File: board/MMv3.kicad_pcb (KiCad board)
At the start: 2 copper layers, 53 parts, among them J1 PWR, J2 SWD, J3 left_mot, J4 DRV8833_L, J5 right_mot, J6 DRV8833_R, Q1 DMG2301L, Q2 DMG2302U, Q3 DMG2302U, Q4 DMG2302U, SW1 but, U1 LSM9DS1, U2 LD1117S50TR_SOT223, U3 DS28E05R+T, U4 RPi_Pico

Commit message: Finished layout
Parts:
- added H1: MountingHole, MountingHole:MountingHole_3.2mm_M3_Pad_TopBottom, F.Cu at (168.0, 95.0)
- D10, D11, D12, D13, D2, D3, D4, D5, D6, D7, D8, D9, J3, J5: moved to B.Cu
- moved Q3 125.1 mm to (165.0, 79.8), turned to 90 degrees
- moved D9 125.1 mm to (166.0, 76.5), turned to 90 degrees
- moved R11 119.3 mm to (165.0, 83.8), turned to 180 degrees
- moved D7 118.7 mm to (166.0, 73.5), turned to 90 degrees
- moved R12 116.1 mm to (165.0, 82.2)
- moved C1 114.9 mm to (173.0, 108.8), turned to 90 degrees
- moved R14 112.5 mm to (168.2, 75.0), turned to 90 degrees
- moved C3 112.4 mm to (167.2, 118.0), turned to 90 degrees
- moved C7 111.7 mm to (171.5, 108.8), turned to 90 degrees
- moved D13 111.3 mm to (177.2, 101.0)
- moved R17 110.4 mm to (178.8, 78.2)
- moved Q4 110.2 mm to (174.0, 75.0)
- moved C2 108.4 mm to (170.0, 108.8), turned to 90 degrees
- moved D12 108.3 mm to (177.2, 76.0)
- moved C5 106.6 mm to (167.5, 112.5), turned to 180 degrees
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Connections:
- J6 pad 2: /lmot_m2 -> /lmot_m1
- J6 pad 3: /lmot_m1 -> /lmot_m2
- J6 pad 4: /rmot_m2 -> /rmot_m1
- J6 pad 5: /rmot_m1 -> /rmot_m2
- R4 pad 2: /r_adc -> /c_adc
- R5 pad 2: /c_adc -> /r_adc
- U4 pad 10: /rir_b -> /lir_b
- U4 pad 11: /rir_en -> /lir_en
- U4 pad 12: /cir_a -> /rir_b
- U4 pad 14: /cir_b -> /rir_a
- U4 pad 15: /cir_en -> /rir_en
- U4 pad 16: /lenc_a -> /cir_a
- U4 pad 17: /lenc_b -> /cir_en
- U4 pad 19: /renc_a -> /cir_b
- U4 pad 20: /renc_b -> Net-(U4-Pad20)
- U4 pad 21: /rmot_in2 -> /lenc_a
- U4 pad 22: /rmot_in1 -> /lenc_b
- U4 pad 24: /lmot_in2 -> /renc_a
- U4 pad 25: /lmot_in1 -> /renc_b
- U4 pad 26: /lir_a -> /rmot_in2
- U4 pad 27: /lir_b -> /rmot_in1
- U4 pad 29: /lir_en -> /lmot_in2
- U4 pad 31: /r_adc -> /c_adc
- U4 pad 32: /c_adc -> /r_adc
- U4 pad 7: Net-(U4-Pad7) -> /lmot_in1
- U4 pad 9: /rir_a -> /lir_a
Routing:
- net +5V: track 0.00 -> 159.0 mm, vias 0 -> 2
- net +3V3: track 0.00 -> 111.8 mm, vias 0 -> 5
- net /r_adc: track 0.00 -> 67.0 mm, vias 0 -> 1
- net /lir_b: track 0.00 -> 63.3 mm
- net /c_adc: track 0.00 -> 61.4 mm
- net /lir_en: track 0.00 -> 55.7 mm, vias 0 -> 1
- net /l_adc: track 0.00 -> 49.5 mm, vias 0 -> 1
- net /lir_a: track 0.00 -> 38.1 mm, vias 0 -> 2
- net Net-(D6-Pad1): track 0.00 -> 36.5 mm
- net /cir_a: track 0.00 -> 34.3 mm
- net /RST: track 0.00 -> 34.1 mm
- net Net-(D2-Pad1): track 0.00 -> 33.1 mm
- net /rmot_in2: track 0.00 -> 33.1 mm
- net /rir_a: track 0.00 -> 33.0 mm
- net Net-(D10-Pad1): track 0.00 -> 32.4 mm
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- added copper zone on B.Cu, net GND
- added copper zone on F.Cu, net GND
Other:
- board outline added: 64 x 54 mm
- net class Power added: clearance 0.2, trace_width 0.32, via_dia 0.6, via_drill 0.3
- board text added: "MMv3 R1 Matthew Tran"

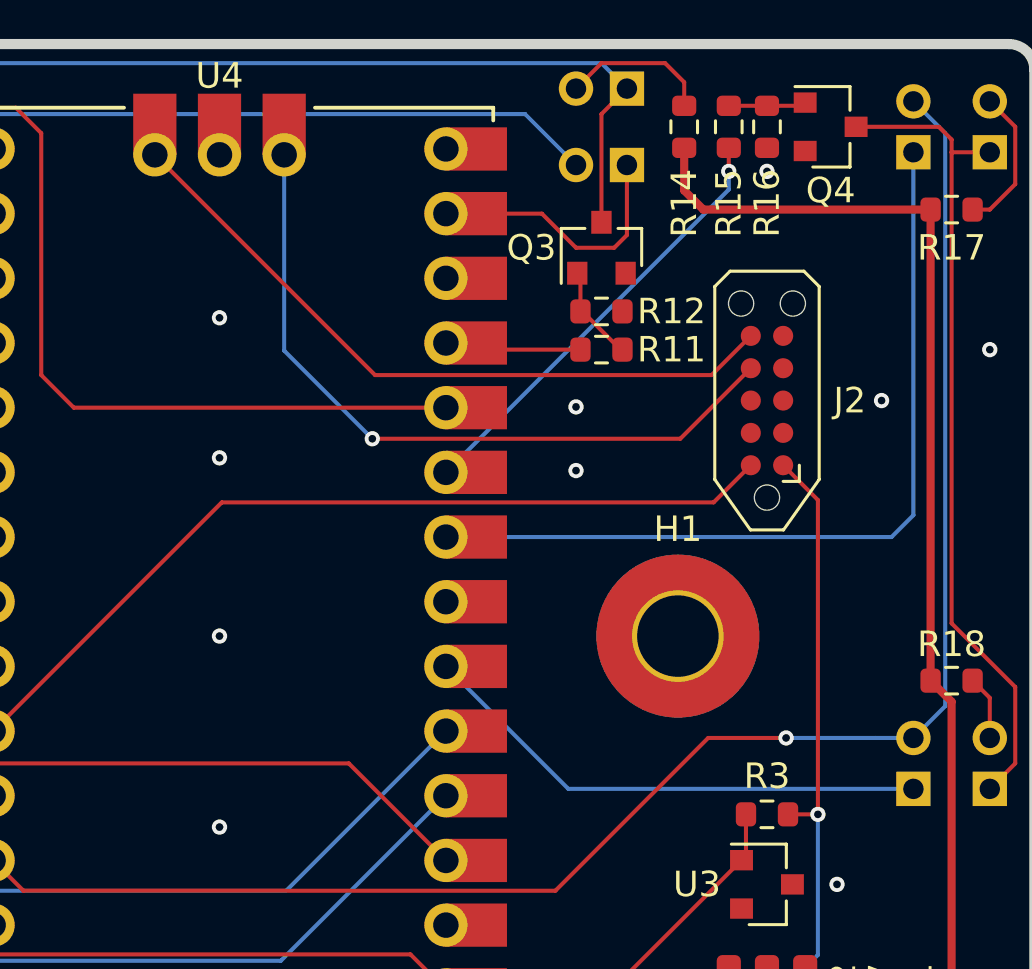
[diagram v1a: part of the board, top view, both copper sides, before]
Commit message: Fixed SWD pinout
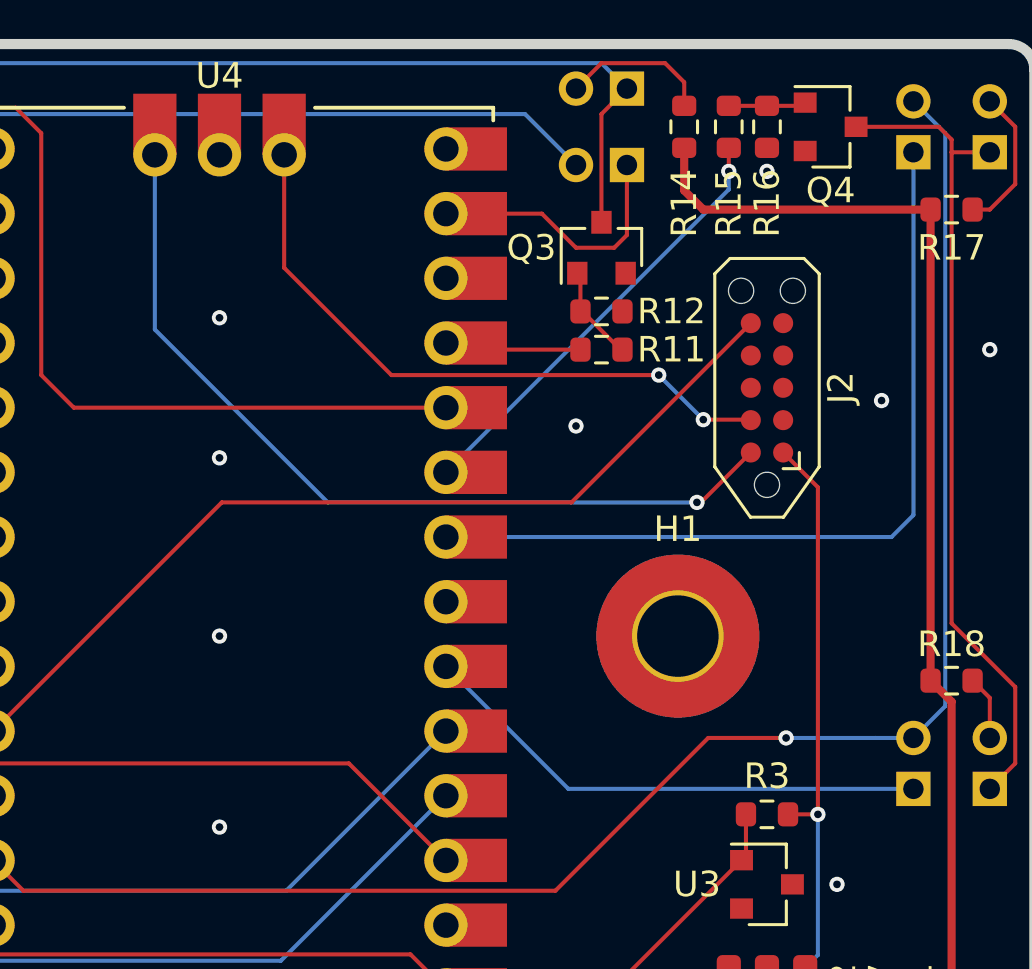
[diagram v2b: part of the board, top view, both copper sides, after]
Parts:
- moved J2 0.50 mm to (171.5, 85.2)
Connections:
- J2 pad 10: /RST -> /SWDIO
- J2 pad 6: /SWDIO -> /RST
- J2 pad 7: /SWCLK -> Net-(J2-Pad7)
- J2 pad 9: Net-(J2-Pad9) -> /SWCLK
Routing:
- net /SWDIO: track 27.6 -> 33.9 mm, vias 0 -> 1
- net /SWCLK: track 28.6 -> 25.2 mm, vias 1 -> 2
- net /RST: track 34.1 -> 36.4 mm
- net +3V3: track 111.8 -> 112.3 mm
- net GND: vias 19 -> 18

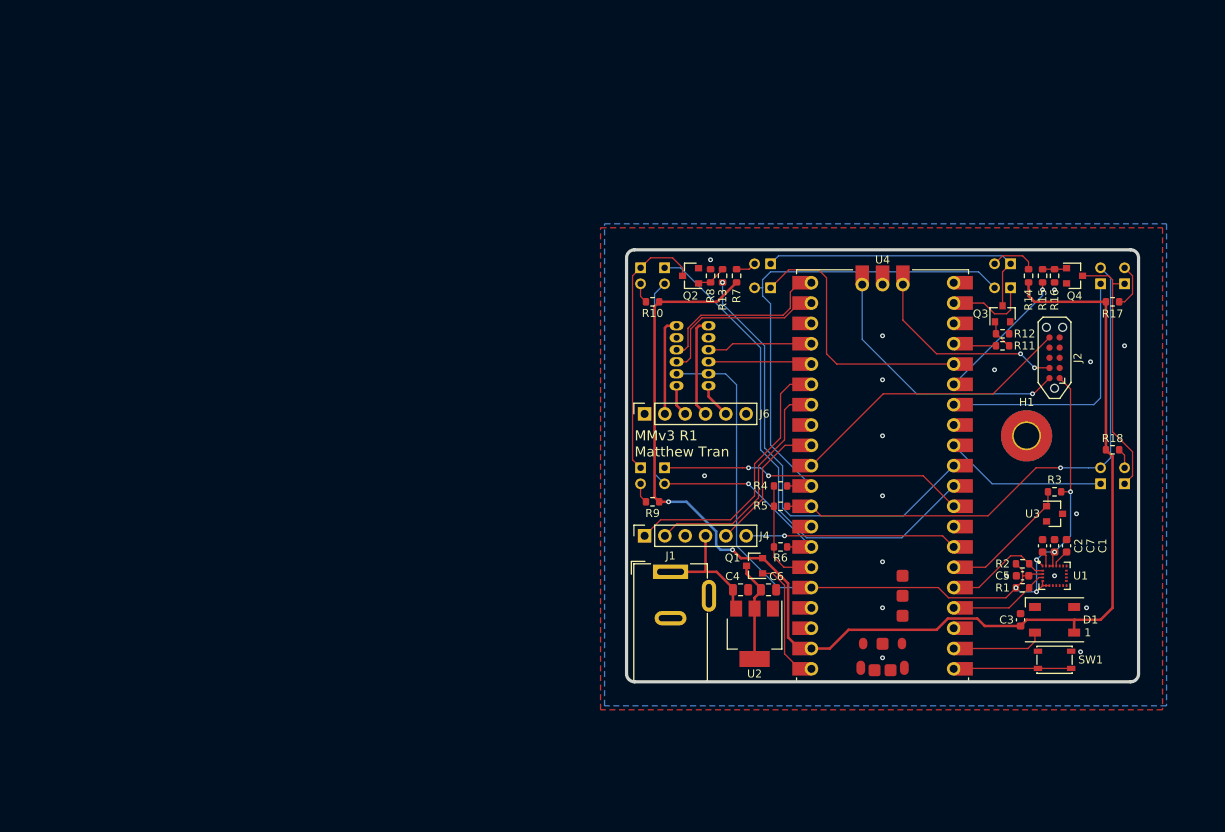
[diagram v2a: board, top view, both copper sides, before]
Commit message: finished mmv3.1 routing
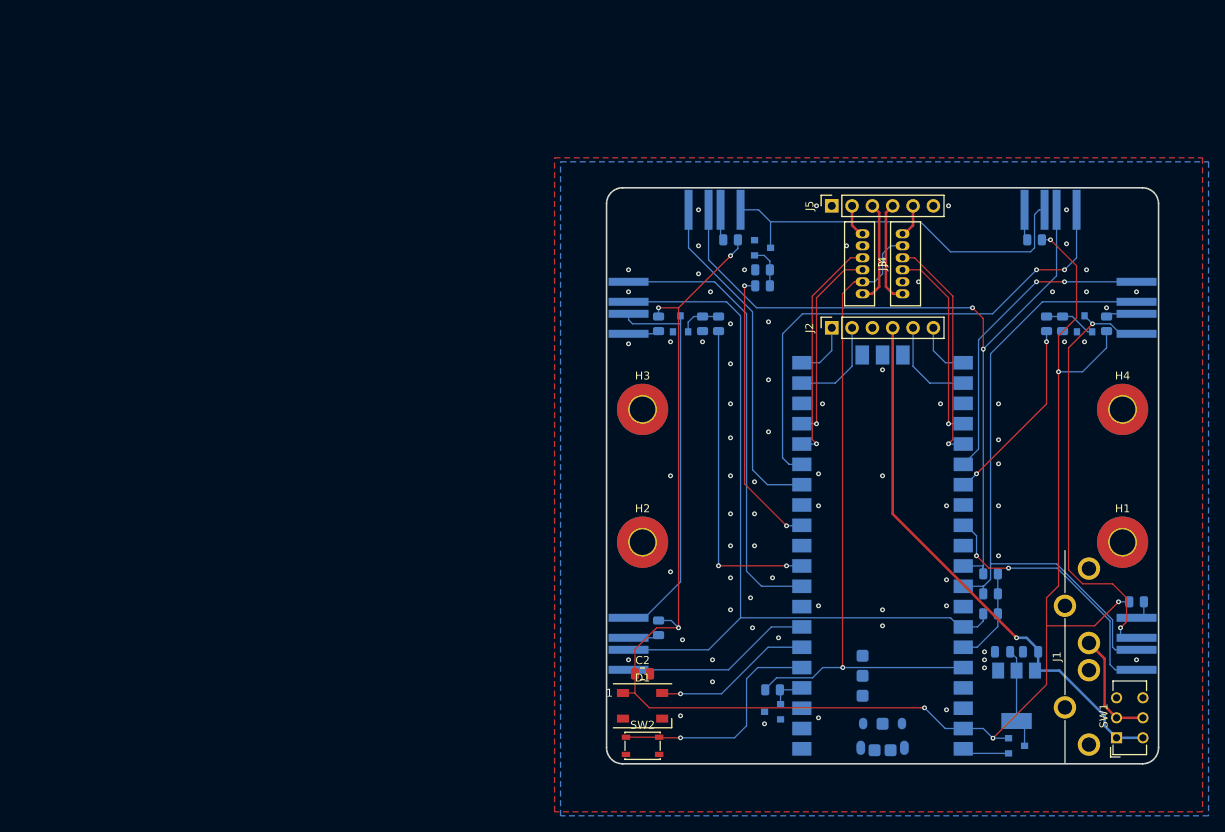
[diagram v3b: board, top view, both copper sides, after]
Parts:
- removed C4, C6: 10u, Capacitor_SMD:C_0805_2012Metric
- removed C5, C7: 100n, Capacitor_SMD:C_0603_1608Metric
- removed J6: DRV8833_R, Connector_PinSocket_2.54mm:PinSocket_1x06_P2.54mm_Vertical
- removed R17, R18: 150, Resistor_SMD:R_0603_1608Metric
- removed U4: RPi_Pico, extraparts:RPi_Pico
- added H2: MountingHole, MountingHole:MountingHole_3.2mm_M3_Pad_TopBottom, F.Cu at (120.0, 108.3)
- added H3: MountingHole, MountingHole:MountingHole_3.2mm_M3_Pad_TopBottom, F.Cu at (120.0, 91.7)
- added H4: MountingHole, MountingHole:MountingHole_3.2mm_M3_Pad_TopBottom, F.Cu at (180.0, 91.7)
- added SW2: but, Button_Switch_SMD:SW_SPST_PTS810, F.Cu at (120.0, 133.8)
- C1: value 10n -> 10u; footprint Capacitor_SMD:C_0603_1608Metric -> Capacitor_SMD:C_0805_2012Metric; moved to B.Cu
- C2: footprint Capacitor_SMD:C_0603_1608Metric -> Capacitor_SMD:C_0805_2012Metric
- C3: value 100n -> 10u; footprint Capacitor_SMD:C_0603_1608Metric -> Capacitor_SMD:C_0805_2012Metric; moved to B.Cu
- D10, D11, D13, D2, D3, D5, D6, D7, D9: footprint Connector_PinHeader_2.00mm:PinHeader_1x02_P2.00mm_Vertical -> extraparts:LED_D3.00mm_RH_SMD
- D12, D4, D8: footprint Connector_PinHeader_2.00mm:PinHeader_1x02_P2.00mm_Vertical -> extraparts:LED_D3.00mm_RH_SMD_ALT
- J1: value PWR -> 9V; footprint Connector_BarrelJack:BarrelJack_Wuerth_6941xx301002 -> extraparts:Keystone_593_594
- J2: value SWD -> DRV8833_L; footprint Connector:Tag-Connect_TC2050-IDC-NL_2x05_P1.27mm_Vertical -> Connector_PinSocket_2.54mm:PinSocket_1x06_P2.54mm_Vertical
- J3: moved to F.Cu
- J4: value DRV8833_L -> right_mot; footprint Connector_PinSocket_2.54mm:PinSocket_1x06_P2.54mm_Vertical -> extraparts:JST_ZH_Vert_6pin
- J5: value right_mot -> DRV8833_R; footprint extraparts:JST_ZH_Vert_6pin -> Connector_PinSocket_2.54mm:PinSocket_1x06_P2.54mm_Vertical; moved to F.Cu
- Q1, Q2, Q3, Q4, U2: moved to B.Cu
- R1, R11, R13, R15, R4, R7, R9: footprint Resistor_SMD:R_0603_1608Metric -> Resistor_SMD:R_0805_2012Metric; moved to B.Cu
- R10, R14: value 150 -> 10k; footprint Resistor_SMD:R_0603_1608Metric -> Resistor_SMD:R_0805_2012Metric; moved to B.Cu
- R12, R16, R8: value 10k -> 150; footprint Resistor_SMD:R_0603_1608Metric -> Resistor_SMD:R_0805_2012Metric; moved to B.Cu
- R2, R3: value 1k -> 1M; footprint Resistor_SMD:R_0603_1608Metric -> Resistor_SMD:R_0805_2012Metric; moved to B.Cu
- R5: value 1M -> 150; footprint Resistor_SMD:R_0603_1608Metric -> Resistor_SMD:R_0805_2012Metric; moved to B.Cu
- R6: value 1M -> 10k; footprint Resistor_SMD:R_0603_1608Metric -> Resistor_SMD:R_0805_2012Metric; moved to B.Cu
- SW1: value but -> PWR; footprint Button_Switch_SMD:SW_SPST_PTS810 -> Button_Switch_THT:SW_CuK_JS202011CQN_DPDT_Straight
- U1: value LSM9DS1 -> DS28E05R+T; footprint Package_LGA:LGA-24L_3x3.5mm_P0.43mm -> Package_TO_SOT_SMD:SOT-23; moved to B.Cu
- U3: value DS28E05R+T -> RPi_Pico; footprint Package_TO_SOT_SMD:SOT-23 -> extraparts:RPi_Pico_SMD; moved to B.Cu
- moved D1 52.6 mm to (120.0, 128.8), turned to 0 degrees
- moved C2 52.5 mm to (120.0, 124.8), turned to 0 degrees
- moved J1 50.4 mm to (172.8, 122.6), turned to 90 degrees
- moved R7 44.7 mm to (122.0, 119.0)
- moved J4 44.2 mm to (152.5, 77.2)
- moved R16 42.0 mm to (181.8, 115.8), turned to 0 degrees
- moved Q1 39.7 mm to (166.8, 133.8), turned to 0 degrees
- moved R13 39.2 mm to (170.5, 81.0), turned to 270 degrees
- moved U1 39.1 mm to (136.2, 129.5), turned to 180 degrees
- moved R11 36.5 mm to (131.0, 70.5)
- moved R1 33.8 mm to (136.2, 126.8)
- moved U2 33.7 mm to (166.8, 127.5)
- moved Q3 31.1 mm to (135.0, 71.5), turned to 0 degrees
- moved R4 30.7 mm to (163.5, 117.2), turned to 180 degrees
- moved R9 30.3 mm to (135.0, 76.2)
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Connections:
- C1 pad 1: Net-(C1-Pad1) -> +9V
- C2 pad 1: Net-(C2-Pad1) -> +5V
- C3 pad 1: +5V -> Net-(C3-Pad1)
- J1 pad 1: +9V -> GND
- J1 pad 2: GND -> Net-(J1-Pad2)
- J2 pad 1: +3V3 -> /rmot_in2
- J2 pad 2: GND -> /rmot_in1
- J2 pad 4: Net-(J2-Pad4) -> +9V
- J2 pad 5: GND -> /lmot_in2
- J2 pad 6: /RST -> /lmot_in1
- J4 pad 1: /rmot_in2 -> /rmot_m1
- J4 pad 2: /rmot_in1 -> GND
- J4 pad 3: GND -> /renc_a
- J4 pad 4: +9V -> /renc_b
- J4 pad 5: /lmot_in2 -> +3V3
- J4 pad 6: /lmot_in1 -> /rmot_m2
- J5 pad 1: /rmot_m1 -> Net-(J5-Pad1)
- J5 pad 2: GND -> /lmot_m1
- J5 pad 3: /renc_a -> /lmot_m2
- J5 pad 4: /renc_b -> /rmot_m1
- J5 pad 5: +3V3 -> /rmot_m2
- J5 pad 6: /rmot_m2 -> Net-(J5-Pad6)
- Q1 pad 3: Net-(C6-Pad1) -> Net-(C3-Pad1)
- R1 pad 2: /sda -> /onewire
- R10 pad 1: +5V -> Net-(Q3-Pad1)
- R10 pad 2: Net-(D3-Pad2) -> GND
- R11 pad 1: Net-(Q3-Pad1) -> +5V
- R11 pad 2: /cir_en -> Net-(D6-Pad2)
- R12 pad 1: Net-(Q3-Pad1) -> +5V
- R12 pad 2: GND -> Net-(D7-Pad2)
- R13 pad 1: +5V -> Net-(Q4-Pad1)
- R13 pad 2: Net-(D6-Pad2) -> /rir_en
- R14 pad 1: +5V -> Net-(Q4-Pad1)
- R14 pad 2: Net-(D7-Pad2) -> GND
- R15 pad 1: Net-(Q4-Pad1) -> +5V
- R15 pad 2: /rir_en -> Net-(D10-Pad2)
- R16 pad 1: Net-(Q4-Pad1) -> +5V
- R16 pad 2: GND -> Net-(D11-Pad2)
- R2 pad 1: +3V3 -> /+3V3A
- R2 pad 2: /scl -> /c_adc
- R3 pad 1: +3V3 -> /+3V3A
- R3 pad 2: /onewire -> /r_adc
- R4 pad 2: /c_adc -> /l_adc
- R5 pad 1: /+3V3A -> Net-(Q2-Pad1)
- R5 pad 2: /r_adc -> /lir_en
- R6 pad 1: /+3V3A -> Net-(Q2-Pad1)
- R6 pad 2: /l_adc -> GND
- R7 pad 1: Net-(Q2-Pad1) -> +5V
- R7 pad 2: /lir_en -> Net-(D2-Pad2)
- R8 pad 1: Net-(Q2-Pad1) -> +5V
- R8 pad 2: GND -> Net-(D3-Pad2)
- R9 pad 1: +5V -> Net-(Q3-Pad1)
- R9 pad 2: Net-(D2-Pad2) -> /cir_en
- SW1 pad 1: /but -> +9V
- SW1 pad 2: GND -> Net-(J1-Pad2)
- U1 pad 1: +3V3 -> /onewire
- U1 pad 2: /scl -> Net-(U1-Pad2)
- U1 pad 3: +3V3 -> GND
- U2 pad 2: Net-(C6-Pad1) -> Net-(C3-Pad1)
- U3 pad 1: /onewire -> Net-(U3-Pad1)
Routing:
- net /cir_b: track 9.42 -> 64.9 mm, vias 0 -> 2
- net +9V: track 15.9 -> 69.0 mm, vias 0 -> 1
- net +5V: track 159.0 -> 210.6 mm, vias 2 -> 8
- net /l_adc: track 49.5 -> 100.2 mm, vias 1 -> 0
- net /c_adc: track 61.4 -> 100.2 mm, vias 0 -> 2
- net /RST: track 36.4 -> 0.00 mm
- net /SWDIO: track 33.9 -> 0.00 mm, vias 1 -> 0
- net /cir_en: track 4.19 -> 35.4 mm, vias 0 -> 2
- net +3V3: track 112.3 -> 84.2 mm, vias 5 -> 1
- net /rmot_in2: track 33.1 -> 7.22 mm
- net /SWCLK: track 25.2 -> 0.00 mm, vias 2 -> 0
- net Net-(D10-Pad1): track 32.4 -> 55.4 mm, vias 0 -> 2
- net /lmot_in1: track 26.5 -> 7.22 mm, vias 1 -> 0
- net /renc_b: track 11.8 -> 28.8 mm, vias 0 -> 1
- net /rmot_in1: track 28.4 -> 12.0 mm
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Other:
- board size 64 x 54 mm -> 69 x 72 mm
- board text removed: "MMv3 R1 Matthew Tran"

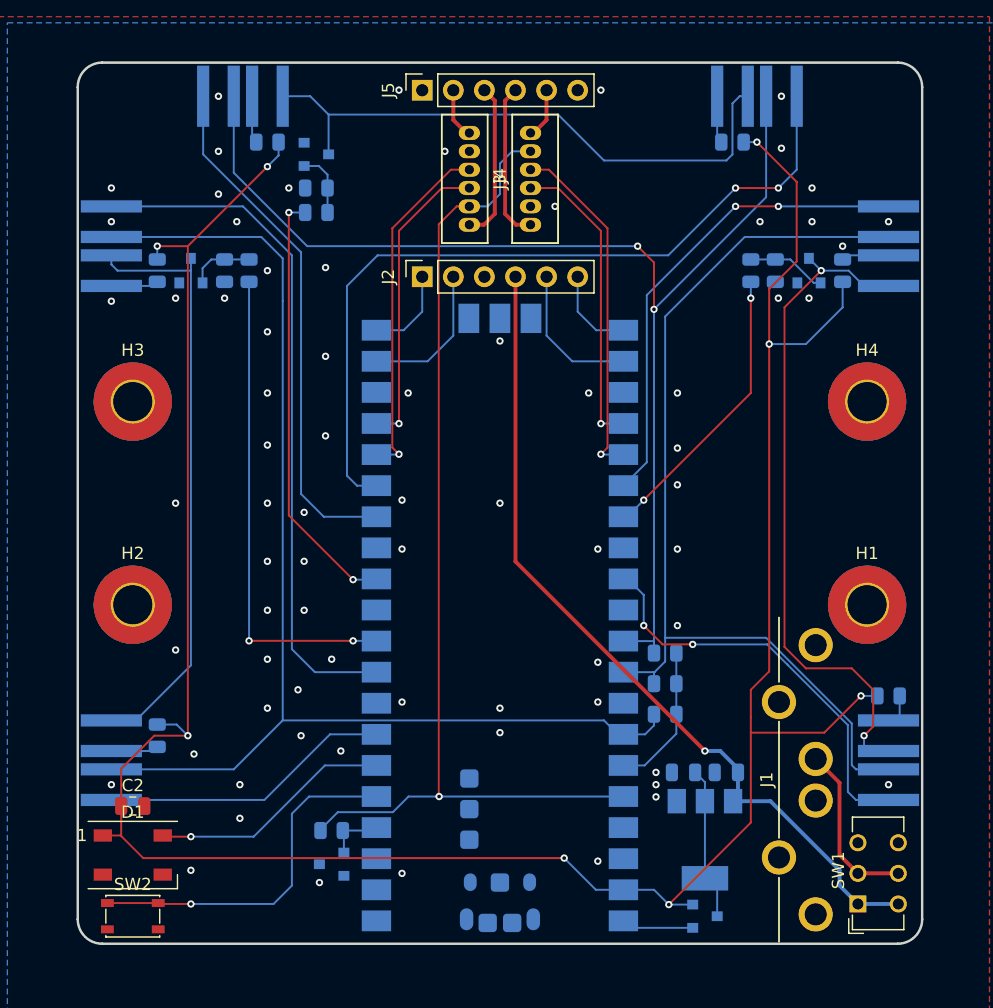
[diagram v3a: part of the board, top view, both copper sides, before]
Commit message: finished MMv3.1 layout
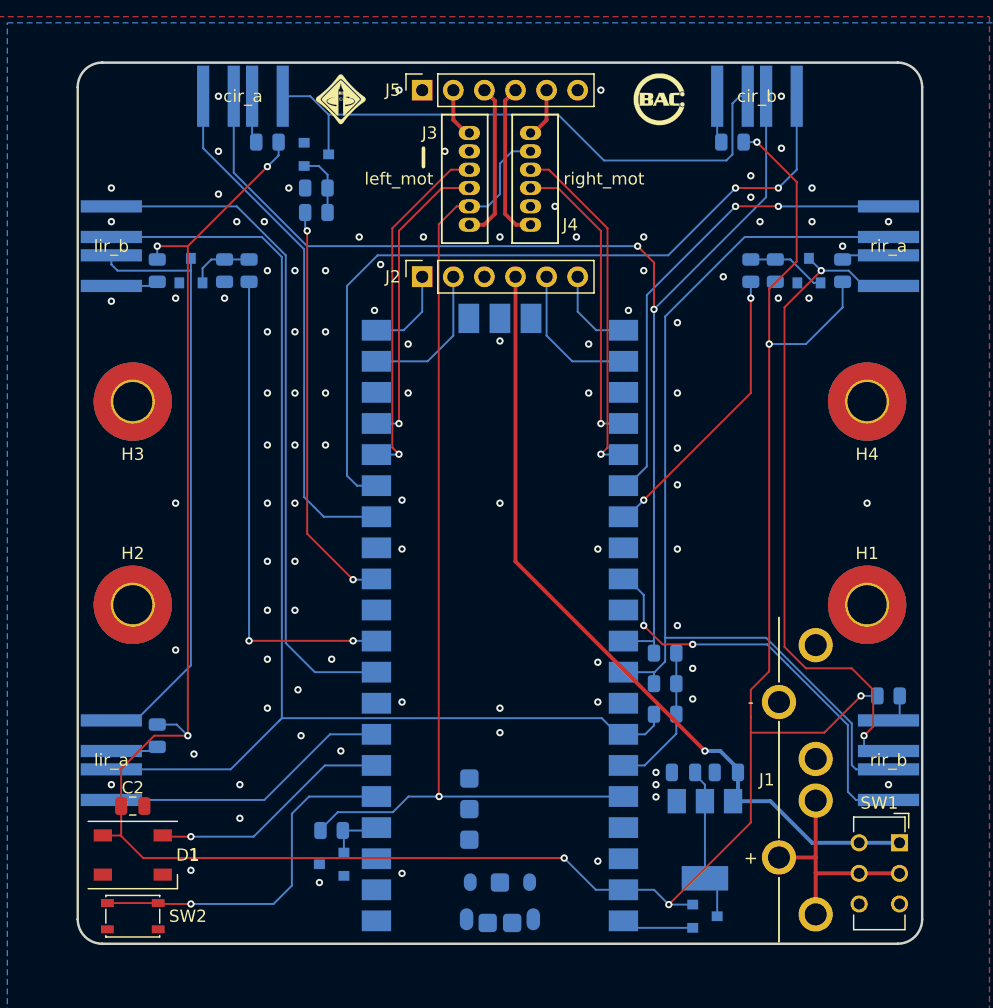
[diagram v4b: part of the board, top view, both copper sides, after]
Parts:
- added H5: bac logo, extraparts:bac_logo, F.Cu at (163.0, 67.0)
- added H6: ieee logo, extraparts:ieee_logo, F.Cu at (137.0, 67.0)
- moved SW1 6.05 mm to (182.7, 127.8), turned to 270 degrees
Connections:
- J1 pad 1: GND -> Net-(J1-Pad1)
- J1 pad 2: Net-(J1-Pad2) -> GND
- SW1 pad 2: Net-(J1-Pad2) -> Net-(J1-Pad1)
- SW1 pad 5: Net-(J1-Pad2) -> Net-(J1-Pad1)
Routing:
- net Net-(J1-Pad1): track 0.00 -> 19.2 mm
- net Net-(J1-Pad2): track 14.1 -> 0.00 mm
- net +9V: track 69.0 -> 66.3 mm
- net /cir_en: track 35.4 -> 33.6 mm
- net /rir_a: track 39.1 -> 38.5 mm
- net GND: vias 73 -> 97
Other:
- board text added: "+"
- board text added: "-"
- board text added: "1wire"
- board text added: "MMv3.1 Matt Tran"
- board text added: "cir_a"
- board text added: "cir_b"
- board text added: "left_mot"
- board text added: "lir_a"
- board text added: "lir_b"
- board text added: "right_mot"
- board text added: "rir_a"
- board text added: "rir_b"
